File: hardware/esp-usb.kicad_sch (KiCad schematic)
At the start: 29 parts, among them J1 USB_A, J2 Conn_01x05, J3 Conn_01x05, J4 USB_A, SW1 SW_Push, U1 ESP32-C3, U2 SPX3819M5-L-3-3, U7 TPD2EUSB30A, Y1 Crystal_GND23

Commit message: Final rev!
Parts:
- C13, C2, C5, C6: LCSC Part # (none) -> C1525
- R1: LCSC Part # (none) -> C25744
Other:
- moved on the sheet: AE1, C10, C2, C3, C4, C5, C6, C7, C8, C9, L1, R1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

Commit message: Use IRL pic
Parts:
- SW1: LCSC Part # C2689695 -> C2764561
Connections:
- net GPIO3: now also D1.2 (A); no longer D1.1 (K)
- net GPIO4: now also D2.2 (A); no longer D2.1 (K)
- net at R3.1: now also D1.1 (K); no longer D1.2 (A)
- net at R2.1: now also D2.1 (K); no longer D2.2 (A)
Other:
- moved on the sheet: D1, D2
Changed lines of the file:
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@@
 			)
 		)
-		(property "LCSC Part #" "C2689695"
+		(property "LCSC Part #" "C2764561"
 			(at 124.46 92.71 0)
 			(effects
@@
 	(symbol
 		(lib_id "Device:LED")
-		(at 93.98 87.63 180)
+		(at 93.98 87.63 0)
+		(mirror x)
 		(unit 1)
 		(exclude_from_sim no)
@@
 	(symbol
 		(lib_id "Device:LED")
-		(at 93.98 81.28 180)
+		(at 93.98 81.28 0)
+		(mirror x)
 		(unit 1)
 		(exclude_from_sim no)

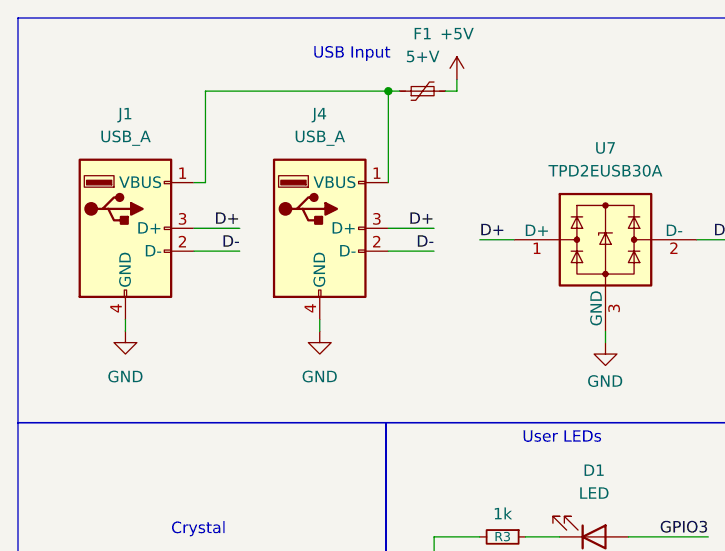
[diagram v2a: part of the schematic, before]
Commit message: Remove back fill
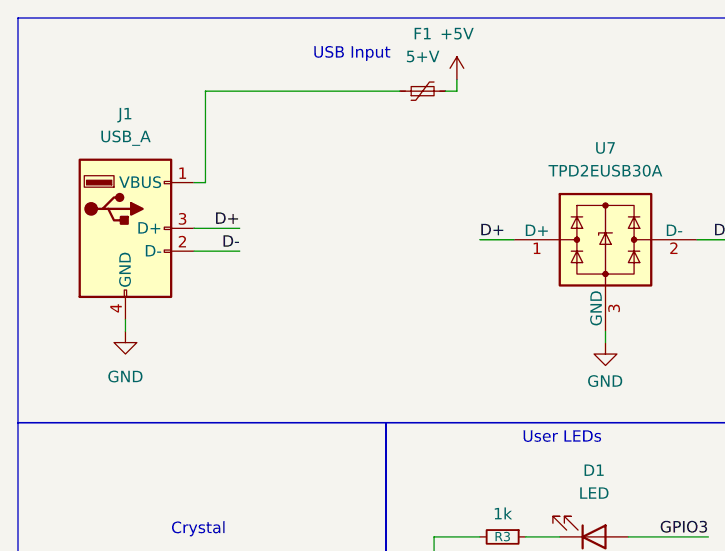
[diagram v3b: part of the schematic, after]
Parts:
- removed J4: USB_A, esp-usb-lib:USBPCB, symbol Connector:USB_A
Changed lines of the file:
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@@
 	)
 	(junction
-		(at 71.12 31.75)
-		(diameter 0)
-		(color 0 0 0 0)
-	)
-	(junction
 		(at 160.02 78.74)
 		(diameter 0)
@@
 	(wire
 		(pts
-			(xy 71.12 31.75) (xy 71.12 41.91)
-		)
-		(stroke
-			(width 0)
-			(type default)
-		)
-	)
-	(wire
-		(pts
 			(xy 58.42 152.4) (xy 71.12 152.4)
 		)
@@
 	(wire
 		(pts
-			(xy 71.12 49.53) (xy 76.2 49.53)
-		)
-		(stroke
-			(width 0)
-			(type default)
-		)
-	)
-	(wire
-		(pts
 			(xy 132.08 97.79) (xy 142.24 97.79)
 		)
@@
 	(wire
 		(pts
-			(xy 50.8 31.75) (xy 71.12 31.75)
-		)
-		(stroke
-			(width 0)
-			(type default)
-		)
-	)
-	(wire
-		(pts
 			(xy 224.79 80.01) (xy 227.33 80.01)
 		)
@@
 	(wire
 		(pts
-			(xy 63.5 57.15) (xy 63.5 58.42)
-		)
-		(stroke
-			(width 0)
-			(type default)
-		)
-	)
-	(wire
-		(pts
 			(xy 132.08 120.65) (xy 142.24 120.65)
 		)
@@
 	(wire
 		(pts
-			(xy 72.39 31.75) (xy 71.12 31.75)
+			(xy 50.8 31.75) (xy 72.39 31.75)
 		)
 		(stroke
@@
 	(wire
 		(pts
-			(xy 71.12 46.99) (xy 76.2 46.99)
-		)
-		(stroke
-			(width 0)
-			(type default)
-		)
-	)
-	(wire
-		(pts
 			(xy 132.08 107.95) (xy 142.24 107.95)
 		)
@@
 		)
 	)
-	(label "D-"
-		(at 76.2 49.53 180)
-		(effects
-			(font
-				(size 1.27 1.27)
-			)
-			(justify right bottom)
-		)
-	)
 	(label "D+"
 		(at 54.61 46.99 180)
@@
 		)
 	)
-	(label "D+"
-		(at 76.2 46.99 180)
-		(effects
-			(font
-				(size 1.27 1.27)
-			)
-			(justify right bottom)
-		)
-	)
 	(label "GPIO4"
 		(at 198.12 95.25 180)
@@
 	(symbol
 		(lib_id "power:GND")
-		(at 63.5 58.42 0)
-		(unit 1)
-		(exclude_from_sim no)
-		(in_bom yes)
-		(on_board yes)
-		(dnp no)
-		(fields_autoplaced yes)
-		(property "Reference" "#PWR021"
-			(at 63.5 64.77 0)
-			(effects
-				(font
-					(size 1.27 1.27)
-				)
-				(hide yes)
-			)
-		)
-		(property "Value" "GND"
-			(at 63.5 63.5 0)
-			(effects
-				(font
-					(size 1.27 1.27)
-				)
-			)
-		)
-		(property "Footprint" ""
-			(at 63.5 58.42 0)
-			(effects
-				(font
-					(size 1.27 1.27)
-				)
-				(hide yes)
-			)
-		)
-		(property "Datasheet" ""
-			(at 63.5 58.42 0)
-			(effects
-				(font
-					(size 1.27 1.27)
-				)
-				(hide yes)
-			)
-		)
-		(property "Description" "Power symbol creates a global label with name \"GND\" , ground"
-			(at 63.5 58.42 0)
-			(effects
-				(font
-					(size 1.27 1.27)
-				)
-				(hide yes)
-			)
-		)
-		(pin "1"
-		)
-		(instances
-			(project "esp-usb"
-				(path "/e4e8ee11-8dc8-47f9-8b1c-f8c497eaffab"
-					(reference "#PWR021")
-					(unit 1)
-				)
-			)
-		)
-	)
-	(symbol
-		(lib_id "power:GND")
 		(at 118.11 93.98 0)
 		(mirror y)
@@
 					(unit 1)
 				)
-			)
-		)
-	)
-	(symbol
-		(lib_id "Connector:USB_A")
-		(at 63.5 46.99 0)
-		(unit 1)
-		(exclude_from_sim no)
-		(in_bom no)
-		(on_board yes)
-		(dnp no)
-		(fields_autoplaced yes)
-		(property "Reference" "J4"
-			(at 63.5 34.29 0)
-			(effects
-				(font
-					(size 1.27 1.27)
-				)
-			)
-		)
-		(property "Value" "USB_A"
-			(at 63.5 36.83 0)
-			(effects
-				(font
-					(size 1.27 1.27)
-				)
-			)
-		)
-		(property "Footprint" "esp-usb-lib:USBPCB"
-			(at 67.31 48.26 0)
-			(effects
-				(font
-					(size 1.27 1.27)
-				)
-				(hide yes)
-			)
-		)
-		(property "Datasheet" "~"
-			(at 67.31 48.26 0)
-			(effects
-				(font
-					(size 1.27 1.27)
-				)
-				(hide yes)
-			)
-		)
-		(property "Description" "USB Type A connector"
-			(at 63.5 46.99 0)
-			(effects
-				(font
-					(size 1.27 1.27)
-				)
-				(hide yes)
-			)
-		)
-		(property "LCSC Part #" ""
-			(at 63.5 46.99 0)
-			(effects
-				(font
-					(size 1.27 1.27)
-				)
-				(hide yes)
-			)
-		)
-		(pin "4"
-		)
-		(pin "1"
-		)
-		(pin "3"
-		)
-		(pin "2"
-		)
-		(instances
-			(project "esp-usb"
-				(path "/e4e8ee11-8dc8-47f9-8b1c-f8c497eaffab"
-					(reference "J4")
-					(unit 1)
-				)
